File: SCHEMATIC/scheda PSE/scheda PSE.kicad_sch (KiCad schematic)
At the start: 4 parts

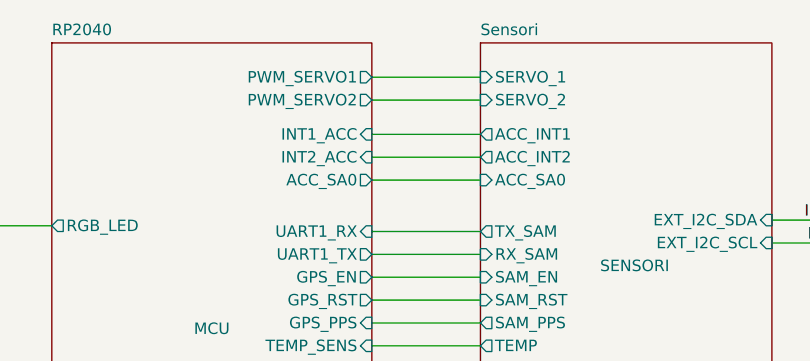
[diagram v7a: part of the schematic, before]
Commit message: Sistemate un po'di cose
aggiuno fori display e terzo servo e sistemate le serigrafie
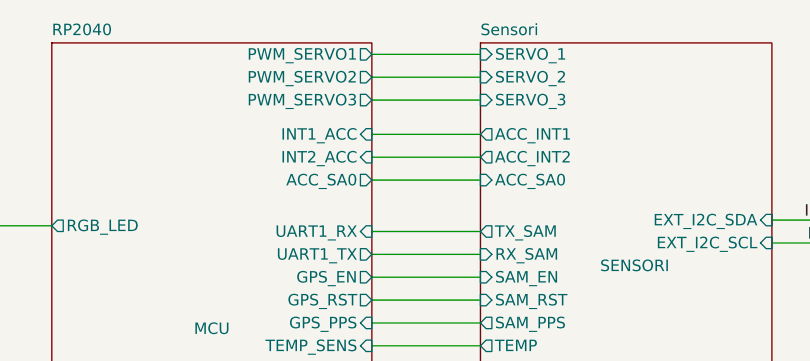
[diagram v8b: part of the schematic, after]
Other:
- sheet RP2040 ports: added PWM_SERVO3; removed none
- sheet Sensori ports: added SERVO_3; removed none
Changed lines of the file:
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@@
+    (stroke (width 0) (type default) (color 0 0 0 0))
+  )
+  (wire (pts (xy 149.86 55.245) (xy 161.925 55.245))
+    (stroke (width 0) (type default) (color 0 0 0 0))
+  )
+  (wire (pts (xy 194.31 73.66) (xy 206.375 73.66))
+    (stroke (width 0) (type default) (color 0 0 0 0))
+  )
+  (wire (pts (xy 149.86 129.54) (xy 161.925 129.54))
+    (stroke (width 0) (type default) (color 0 0 0 0))
+  )
+  (wire (pts (xy 149.86 60.325) (xy 161.925 60.325))
+    (stroke (width 0) (type default) (color 0 0 0 0))
+  )
+  (wire (pts (xy 194.31 96.52) (xy 206.375 96.52))
+    (stroke (width 0) (type default) (color 0 0 0 0))
+  )
+  (wire (pts (xy 103.505 117.475) (xy 114.3 117.475))
+    (stroke (width 0) (type default) (color 0 0 0 0))
+  )
+  (wire (pts (xy 149.86 116.205) (xy 161.925 116.205))
+    (stroke (width 0) (type default) (color 0 0 0 0))
+  )
+  (wire (pts (xy 149.86 126.365) (xy 161.925 126.365))
+    (stroke (width 0) (type default) (color 0 0 0 0))
+  )
+  (wire (pts (xy 149.86 80.01) (xy 161.925 80.01))
+    (stroke (width 0) (type default) (color 0 0 0 0))
+  )
+  (wire (pts (xy 103.505 74.295) (xy 114.3 74.295))
+    (stroke (width 0) (type default) (color 0 0 0 0))
+  )
+  (wire (pts (xy 103.505 124.46) (xy 114.3 124.46))
+    (stroke (width 0) (type default) (color 0 0 0 0))
+  )
+  (wire (pts (xy 103.505 127) (xy 114.3 127))
+    (stroke (width 0) (type default) (color 0 0 0 0))
+  )
+  (wire (pts (xy 149.86 113.665) (xy 161.925 113.665))
+    (stroke (width 0) (type default) (color 0 0 0 0))
+  )
+  (wire (pts (xy 149.86 96.52) (xy 161.925 96.52))
+    (stroke (width 0) (type default) (color 0 0 0 0))
+  )
+  (wire (pts (xy 103.505 120.015) (xy 114.3 120.015))
+    (stroke (width 0) (type default) (color 0 0 0 0))
+  )
+  (wire (pts (xy 70.485 118.11) (xy 74.93 118.11))
+    (stroke (width 0) (type default) (color 0 0 0 0))
+  )
+  (wire (pts (xy 70.485 110.49) (xy 114.3 110.49))
+    (stroke (width 0) (type default) (color 0 0 0 0))
+  )
+  (wire (pts (xy 194.31 76.2) (xy 206.375 76.2))
+    (stroke (width 0) (type default) (color 0 0 0 0))
+  )
+  (wire (pts (xy 149.86 82.55) (xy 161.925 82.55))
+    (stroke (width 0) (type default) (color 0 0 0 0))
+  )
+  (wire (pts (xy 70.485 110.49) (xy 70.485 118.11))
+    (stroke (width 0) (type default) (color 0 0 0 0))
+  )
+  (wire (pts (xy 149.86 69.215) (xy 161.925 69.215))
+    (stroke (width 0) (type default) (color 0 0 0 0))
+  )
+  (wire (pts (xy 149.86 106.045) (xy 161.925 106.045))
+    (stroke (width 0) (type default) (color 0 0 0 0))
+  )
+  (wire (pts (xy 149.86 118.745) (xy 161.925 118.745))
+    (stroke (width 0) (type default) (color 0 0 0 0))
+  )
+  (wire (pts (xy 149.86 64.135) (xy 161.925 64.135))
     (stroke (width 0) (type default) (color 0 0 0 0))
   )
   (wire (pts (xy 149.86 57.785) (xy 161.925 57.785))
-    (stroke (width 0) (type default) (color 0 0 0 0))
-  )
-  (wire (pts (xy 194.31 73.66) (xy 206.375 73.66))
-    (stroke (width 0) (type default) (color 0 0 0 0))
-  )
-  (wire (pts (xy 149.86 129.54) (xy 161.925 129.54))
-    (stroke (width 0) (type default) (color 0 0 0 0))
-  )
-  (wire (pts (xy 194.31 96.52) (xy 206.375 96.52))
-    (stroke (width 0) (type default) (color 0 0 0 0))
-  )
-  (wire (pts (xy 103.505 117.475) (xy 114.3 117.475))
-    (stroke (width 0) (type default) (color 0 0 0 0))
-  )
-  (wire (pts (xy 149.86 116.205) (xy 161.925 116.205))
-    (stroke (width 0) (type default) (color 0 0 0 0))
-  )
-  (wire (pts (xy 149.86 126.365) (xy 161.925 126.365))
-    (stroke (width 0) (type default) (color 0 0 0 0))
-  )
-  (wire (pts (xy 149.86 80.01) (xy 161.925 80.01))
-    (stroke (width 0) (type default) (color 0 0 0 0))
-  )
-  (wire (pts (xy 103.505 74.295) (xy 114.3 74.295))
-    (stroke (width 0) (type default) (color 0 0 0 0))
-  )
-  (wire (pts (xy 103.505 124.46) (xy 114.3 124.46))
-    (stroke (width 0) (type default) (color 0 0 0 0))
-  )
-  (wire (pts (xy 103.505 127) (xy 114.3 127))
-    (stroke (width 0) (type default) (color 0 0 0 0))
-  )
-  (wire (pts (xy 149.86 113.665) (xy 161.925 113.665))
-    (stroke (width 0) (type default) (color 0 0 0 0))
-  )
-  (wire (pts (xy 149.86 96.52) (xy 161.925 96.52))
-    (stroke (width 0) (type default) (color 0 0 0 0))
-  )
-  (wire (pts (xy 103.505 120.015) (xy 114.3 120.015))
-    (stroke (width 0) (type default) (color 0 0 0 0))
-  )
-  (wire (pts (xy 70.485 118.11) (xy 74.93 118.11))
-    (stroke (width 0) (type default) (color 0 0 0 0))
-  )
-  (wire (pts (xy 70.485 110.49) (xy 114.3 110.49))
-    (stroke (width 0) (type default) (color 0 0 0 0))
-  )
-  (wire (pts (xy 194.31 76.2) (xy 206.375 76.2))
-    (stroke (width 0) (type default) (color 0 0 0 0))
-  )
-  (wire (pts (xy 149.86 82.55) (xy 161.925 82.55))
-    (stroke (width 0) (type default) (color 0 0 0 0))
-  )
-  (wire (pts (xy 70.485 110.49) (xy 70.485 118.11))
-    (stroke (width 0) (type default) (color 0 0 0 0))
-  )
-  (wire (pts (xy 149.86 69.215) (xy 161.925 69.215))
-    (stroke (width 0) (type default) (color 0 0 0 0))
-  )
-  (wire (pts (xy 149.86 106.045) (xy 161.925 106.045))
-    (stroke (width 0) (type default) (color 0 0 0 0))
-  )
-  (wire (pts (xy 149.86 118.745) (xy 161.925 118.745))
-    (stroke (width 0) (type default) (color 0 0 0 0))
-  )
-  (wire (pts (xy 149.86 64.135) (xy 161.925 64.135))
-    (stroke (width 0) (type default) (color 0 0 0 0))
-  )
-  (wire (pts (xy 149.86 60.325) (xy 161.925 60.325))
     (stroke (width 0) (type default) (color 0 0 0 0))
   )
@@
       (effects (font (size 1.27 1.27)) (justify left))
     )
-    (pin "SERVO_1" input (at 161.925 57.785 180)
-      (effects (font (size 1.27 1.27)) (justify left))
-    )
-    (pin "SERVO_2" input (at 161.925 60.325 180)
+    (pin "SERVO_1" input (at 161.925 55.245 180)
+      (effects (font (size 1.27 1.27)) (justify left))
+    )
+    (pin "SERVO_2" input (at 161.925 57.785 180)
+      (effects (font (size 1.27 1.27)) (justify left))
+    )
+    (pin "SERVO_3" input (at 161.925 60.325 180)
       (effects (font (size 1.27 1.27)) (justify left))
     )
@@
       (effects (font (size 1.27 1.27)) (justify left))
     )
-    (pin "PWM_SERVO1" output (at 149.86 57.785 0)
-      (effects (font (size 1.27 1.27)) (justify right))
-    )
-    (pin "PWM_SERVO2" output (at 149.86 60.325 0)
+    (pin "PWM_SERVO1" output (at 149.86 55.245 0)
+      (effects (font (size 1.27 1.27)) (justify right))
+    )
+    (pin "PWM_SERVO2" output (at 149.86 57.785 0)
+      (effects (font (size 1.27 1.27)) (justify right))
+    )
+    (pin "PWM_SERVO3" output (at 149.86 60.325 0)
       (effects (font (size 1.27 1.27)) (justify right))
     )
@@
       (reference "#PWR0103") (unit 1) (value "GND") (footprint "")
     )
+    (path "/7389e30f-cc4a-4964-bca3-cd95052ca62a/97a4718d-9276-4c8f-a45e-c503acbe4e3b"
+      (reference "#PWR0104") (unit 1) (value "+5V") (footprint "")
+    )
+    (path "/7389e30f-cc4a-4964-bca3-cd95052ca62a/f1354e6e-3bb1-4820-9642-f5f11f4faa33"
+      (reference "#PWR0105") (unit 1) (value "GND") (footprint "")
+    )
     (path "/79aec321-3c99-4e59-b384-4589f6950bd0/843d4752-6e63-4d95-a426-482380d37ea8"
       (reference "BZ1") (unit 1) (value "Buzzer") (footprint "_PSE:MLT-8530")
@@
       (reference "J9") (unit 1) (value "SERVO_2") (footprint "Connector_PinHeader_2.54mm:PinHeader_1x03_P2.54mm_Vertical")
     )
+    (path "/7389e30f-cc4a-4964-bca3-cd95052ca62a/966c9b94-8731-45f3-969b-2ff8f16c1a87"
+      (reference "J10") (unit 1) (value "SERVO_3") (footprint "Connector_PinHeader_2.54mm:PinHeader_1x03_P2.54mm_Vertical")
+    )
     (path "/788fccce-441b-4b47-abec-e22400b84986/99601af0-6fbe-463b-86cb-069f9233e982"
